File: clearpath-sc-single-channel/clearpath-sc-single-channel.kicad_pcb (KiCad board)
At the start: 2 copper layers, 75 x 50 mm, 58 parts, among them P1 MOLEX_MICROFIT_JR_RH_2x1_WAY, P2 MOLEX_MICROFIT_JR_RH_2x2_WAY, P3 MOLEX_MICROFIT_JR_RH_2x2_WAY, P4 MOLEX_MICROFIT_JR_RH_2x4_WAY, P5 CONN_01X08, Q1 MMBT5401, Q2 MMBTA06, U1 LM317LCPK, U2 FT230XS-R, U3 USBLC6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

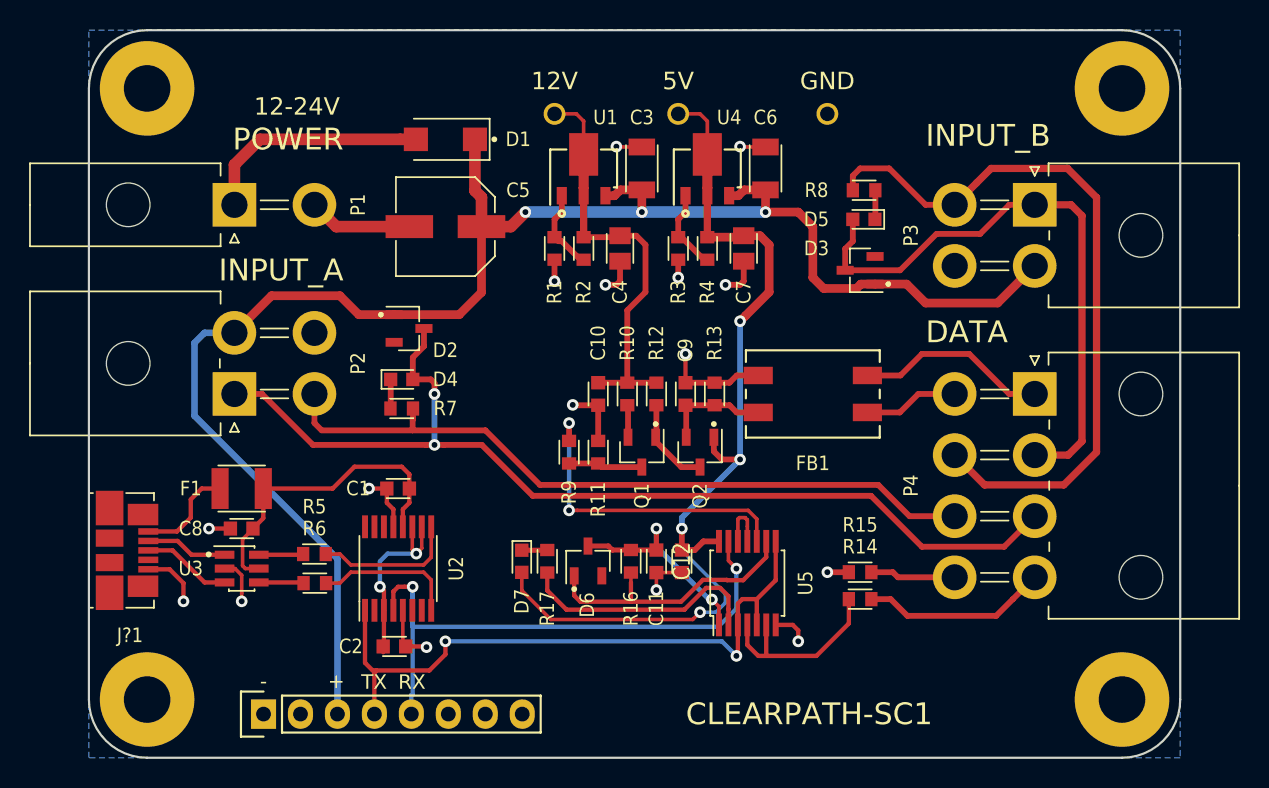
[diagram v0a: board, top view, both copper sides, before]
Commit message: Shrunk board outline slightly to improve tolerances
Useful if mated to a backplane, would allow two within a 100mm long edge area.
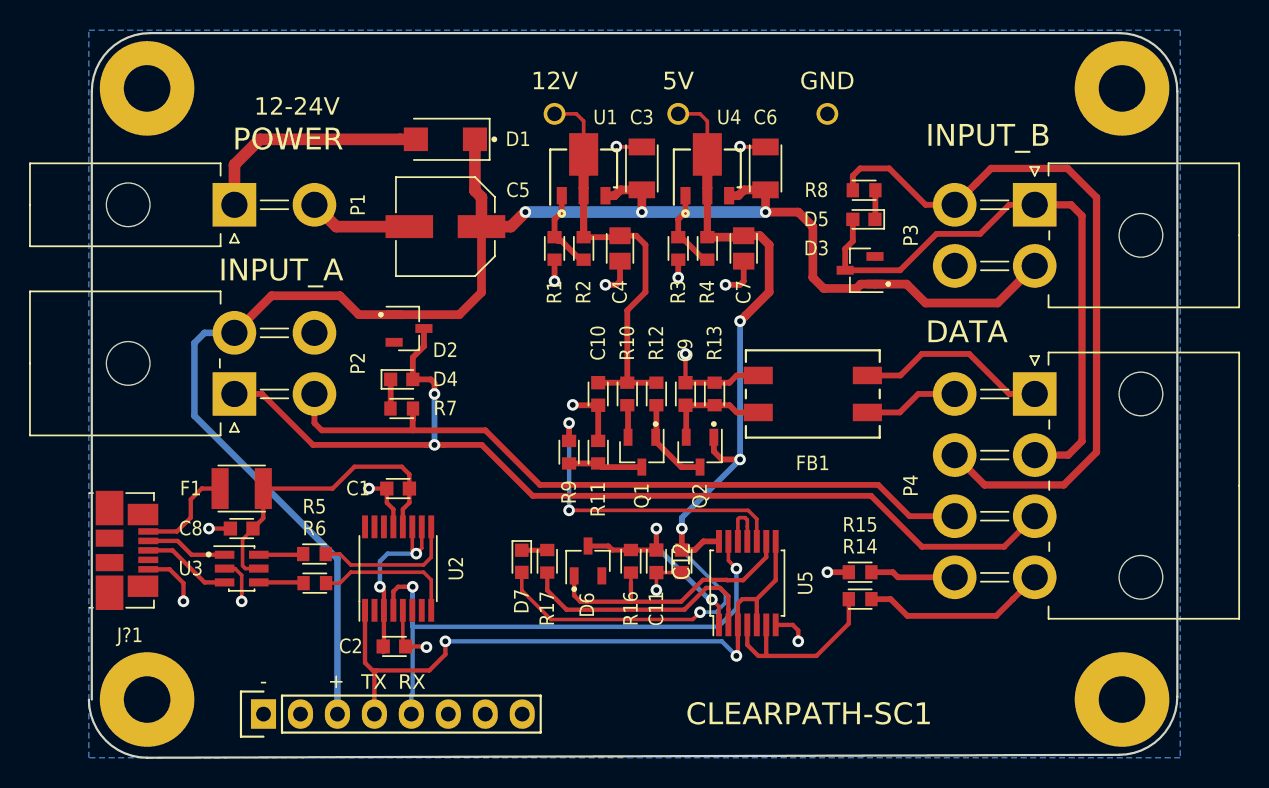
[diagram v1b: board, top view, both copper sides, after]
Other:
- board size 75 x 50 mm -> 74.8 x 49.8 mm
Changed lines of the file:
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@@
     (arrow2b (pts (xy 100 87.5) (xy 101.126504 86.913579)))
   )
-  (gr_arc (start 171 104) (end 175 104) (angle -90) (layer Edge.Cuts) (width 0.15))
-  (gr_arc (start 171 146) (end 171 150) (angle -90) (layer Edge.Cuts) (width 0.15))
+  (gr_arc (start 170.8 104.2) (end 174.8 104.2) (angle -90) (layer Edge.Cuts) (width 0.15))
+  (gr_arc (start 170.8 145.8) (end 170.8 149.8) (angle -90) (layer Edge.Cuts) (width 0.15))
   (gr_arc (start 104 146) (end 100 146) (angle -90) (layer Edge.Cuts) (width 0.15))
-  (gr_arc (start 104 104) (end 100 104) (angle 90) (layer Edge.Cuts) (width 0.15))
-  (gr_line (start 175 146) (end 175 104) (layer Edge.Cuts) (width 0.15))
-  (gr_line (start 104 150) (end 171 150) (layer Edge.Cuts) (width 0.15))
-  (gr_line (start 100 104) (end 100 146) (layer Edge.Cuts) (width 0.15))
-  (gr_line (start 104 100) (end 171 100) (layer Edge.Cuts) (width 0.15))
+  (gr_arc (start 104.2 104.2) (end 100.2 104.2) (angle 90) (layer Edge.Cuts) (width 0.15))
+  (gr_line (start 174.8 145.8) (end 174.8 104.2) (layer Edge.Cuts) (width 0.15))
+  (gr_line (start 104 150) (end 170.8 149.8) (layer Edge.Cuts) (width 0.15))
+  (gr_line (start 100.2 104.2) (end 100.2 146) (layer Edge.Cuts) (width 0.15))
+  (gr_line (start 104.2 100.2) (end 170.8 100.2) (layer Edge.Cuts) (width 0.15))
   (segment (start 111.985 131.5) (end 116.75 131.5) (width 0.3) (layer F.Cu) (net 1))
   (segment (start 116.75 131.5) (end 118.25 130) (width 0.3) (layer F.Cu) (net 1))
